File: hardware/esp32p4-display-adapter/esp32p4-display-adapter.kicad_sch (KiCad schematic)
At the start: 5 parts, among them J1 ESP32-P4_DSI_22pin, J2 Display_30pin, U1 AP2127K-2.8, U2 AP2127K-1.8, U3 TXB0102

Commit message: Fix KiCad schematic syntax (remove comments)
KiCad 8 doesn't accept ;; comments in .kicad_sch files.
Regenerated with proper S-expression format and embedded lib_symbols.
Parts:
- removed U3: TXB0102, Package_SON:Texas_DSBGA-6_0.9x1.4mm_Layout2x3_P0.5mm, symbol Logic_LevelTranslator:TXB0102DCU
- added U3: TXB0102, Package_SO:VSSOP-8_2.3x2mm_P0.5mm, symbol Logic_LevelTranslator:TXB0102
- J1: value ESP32-P4_DSI_22pin -> ESP32-P4_DSI; footprint Connector_FFC-FPC:TE_1-84953-2_1x22-1MP_P0.50mm_Horizontal -> Connector_FFC-FPC:Hirose_FH12-22S-0.5SH_1x22-1MP_P0.50mm_Horizontal
- J2: footprint Connector_FFC-FPC:TE_1-84953-0_1x30-1MP_P0.50mm_Horizontal -> Connector_FFC-FPC:Hirose_FH12-30S-0.5SH_1x30-1MP_P0.50mm_Horizontal
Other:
- note added: "ESP32-P4 DSI to Round Display Adapter MIPI DSI Connections: J1.13/14 (CLK) -> J2.16/17 (TCP/TCN) J1.16/17 (D1) -> J2.13/14 (DIP/DIN) J1.19/20 (D0) -> J2.10/11 (DOP/DON) I2C: J1.2/3 -> J2.25/26 RESET: via U3 level shifter"
- note removed: "ESP32-P4 DSI Connector (22-pin, 0.5mm pitch) J1 - Input from ESP32-P4 DevKit"
- note removed: "Level Shifter: 3.3V ↔ 1.8V for RESET signals"
- note removed: "MIPI DSI Connections: CLK: J1.13/14 → J2.16/17 D0: J1.19/20 → J2.10/11 D1: J1.16/17 → J2.13/14"
- note removed: "Power: 3.3V → LDOs → 2.8V (VCI) + 1.8V (IOVCC)"
- note removed: "Round Display Connector (30-pin, 0.5mm pitch) J2 - Output to QT021WQT Display"

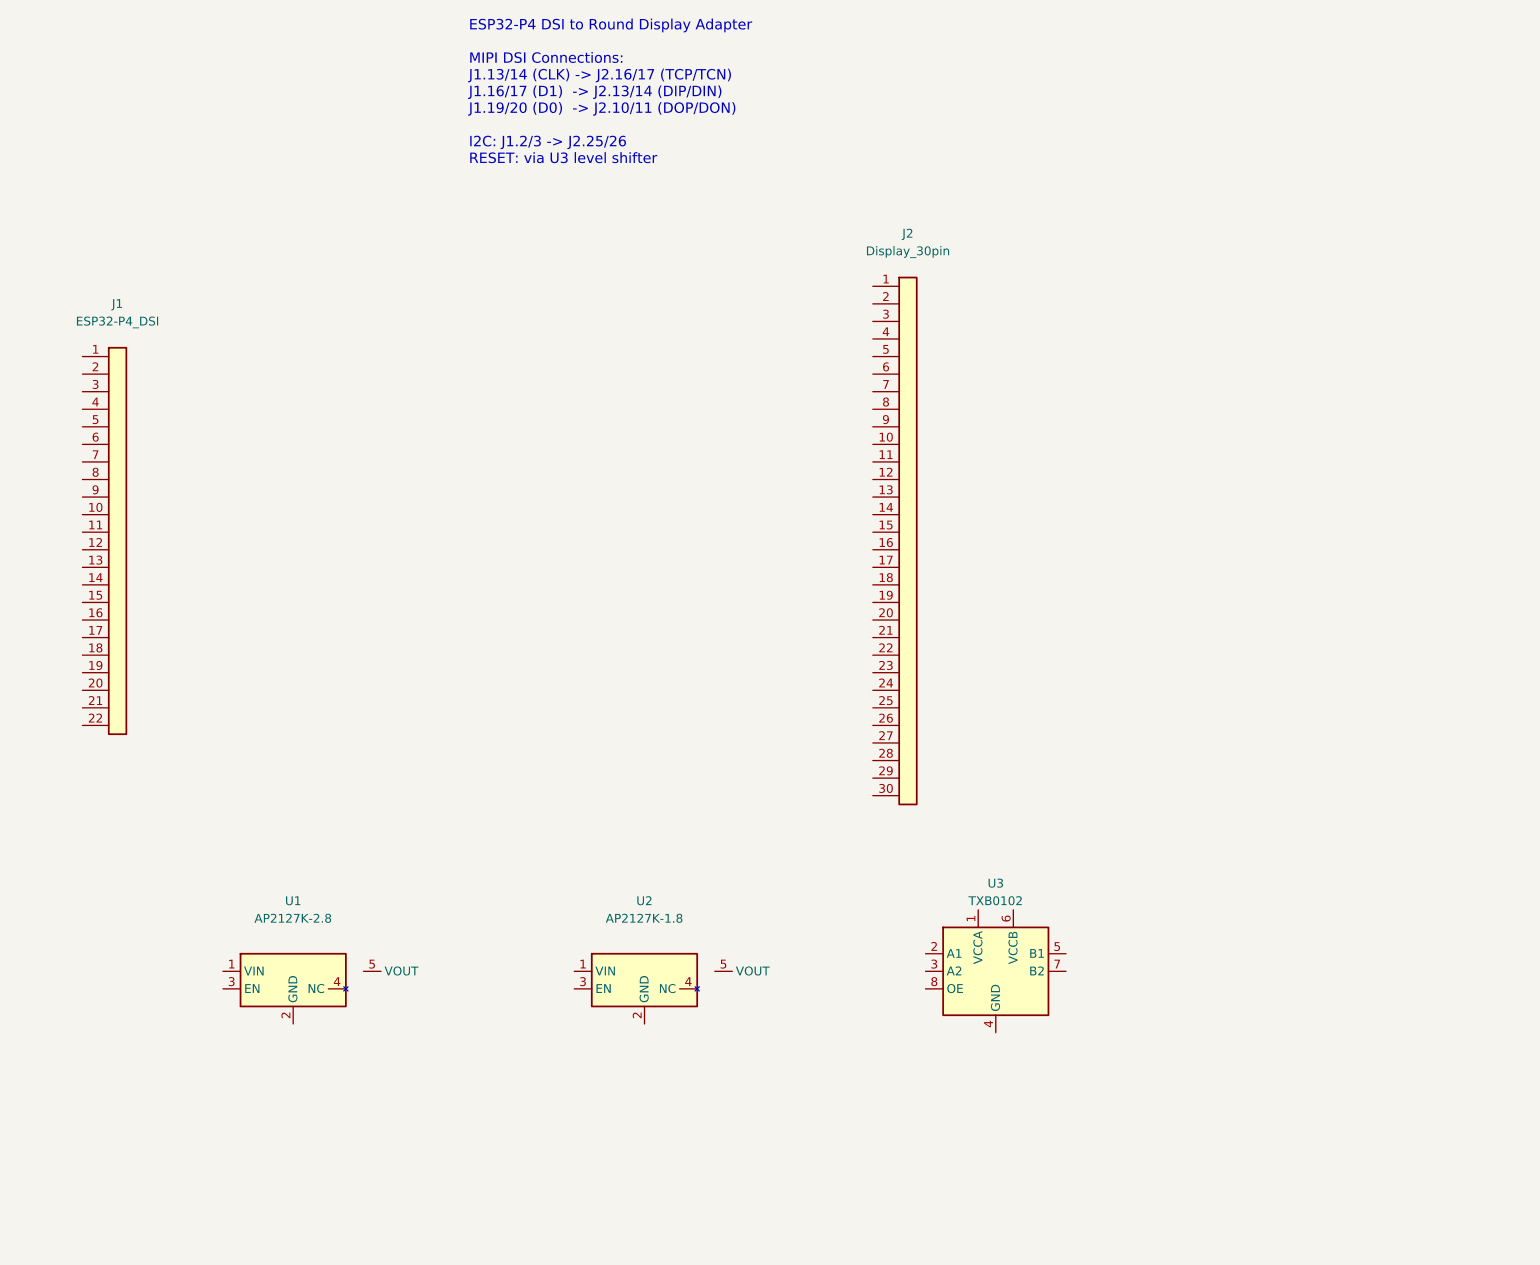
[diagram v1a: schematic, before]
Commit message: Fix ESP32-P4 DSI pinout: 15-pin 1.0mm (same as RPi)
- J1 now 15-pin 1.0mm FPC (was incorrectly 22-pin 0.5mm)
- Added J3 GPIO header for RESET/TP_RESET signals
- Updated pin mapping table to match actual pinout
- Board size 25x30mm
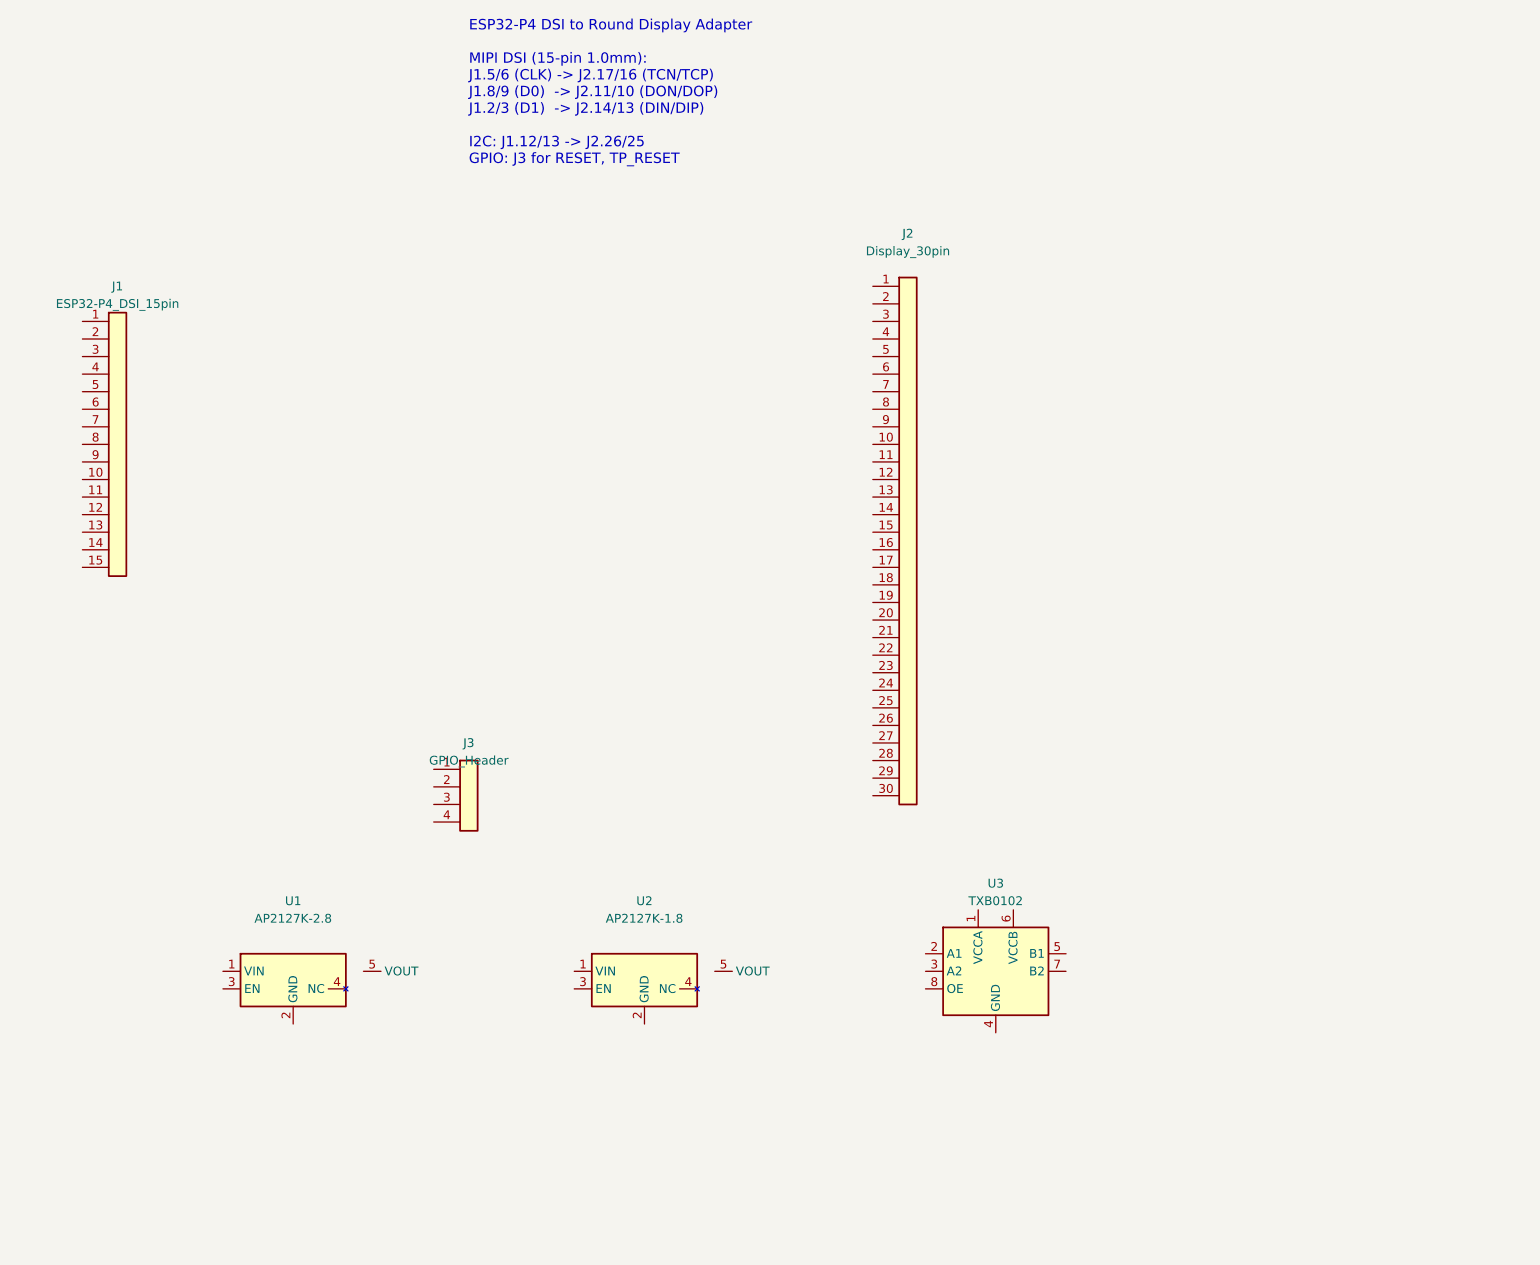
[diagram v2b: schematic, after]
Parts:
- added U3: TXB0102, Package_SO:VSSOP-8_2.3x2mm_P0.5mm, symbol Logic_LevelTranslator:TXB0102
- J1: value ESP32-P4_DSI -> ESP32-P4_DSI_15pin; footprint Connector_FFC-FPC:Hirose_FH12-22S-0.5SH_1x22-1MP_P0.50mm_Horizontal -> Connector_FFC-FPC:Hirose_FH12-15S-1.0SH_1x15-1MP_P1.00mm_Horizontal; symbol Connector_Generic:Conn_01x22 -> Connector_Generic:Conn_01x15
- J3: renamed from U1; value AP2127K-2.8 -> GPIO_Header; footprint Package_TO_SOT_SMD:SOT-23-5 -> Connector_PinHeader_2.54mm:PinHeader_1x04_P2.54mm_Vertical; symbol Regulator_Linear:AP2127K-2.8 -> Connector_Generic:Conn_01x04
- U1: renamed from U2; value AP2127K-1.8 -> AP2127K-2.8; symbol Regulator_Linear:AP2127K-1.8 -> Regulator_Linear:AP2127K-2.8
- U2: renamed from U3; value TXB0102 -> AP2127K-1.8; footprint Package_SO:VSSOP-8_2.3x2mm_P0.5mm -> Package_TO_SOT_SMD:SOT-23-5; symbol Logic_LevelTranslator:TXB0102 -> Regulator_Linear:AP2127K-1.8
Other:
- note added: "ESP32-P4 DSI to Round Display Adapter MIPI DSI (15-pin 1.0mm): J1.5/6 (CLK) -> J2.17/16 (TCN/TCP) J1.8/9 (D0) -> J2.11/10 (DON/DOP) J1.2/3 (D1) -> J2.14/13 (DIN/DIP) I2C: J1.12/13 -> J2.26/25 GPIO: J3 for RESET, TP_RESET"
- note removed: "ESP32-P4 DSI to Round Display Adapter MIPI DSI Connections: J1.13/14 (CLK) -> J2.16/17 (TCP/TCN) J1.16/17 (D1) -> J2.13/14 (DIP/DIN) J1.19/20 (D0) -> J2.10/11 (DOP/DON) I2C: J1.2/3 -> J2.25/26 RESET: via U3 level shifter"
- moved on the sheet: U1
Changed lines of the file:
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@@
     (title "ESP32-P4 DSI to Round Display Adapter")
     (date "2026-04-24")
-    (rev "1.0")
+    (rev "1.1")
     (company "bimmerz.app / OpenCluster")
   )
   (symbol
-    (lib_id "Connector_Generic:Conn_01x22")
-    (at 38.1 88.9 0)
+    (lib_id "Connector_Generic:Conn_01x15")
+    (at 38.1 76.2 0)
     (unit 1)
     (exclude_from_sim no)
@@
     (on_board yes)
     (dnp no)
-    (property "Reference" "J1" (at 38.1 55.88 0) (effects (font (size 1.27 1.27))))
-    (property "Value" "ESP32-P4_DSI" (at 38.1 58.42 0) (effects (font (size 1.27 1.27))))
-    (property "Footprint" "Connector_FFC-FPC:Hirose_FH12-22S-0.5SH_1x22-1MP_P0.50mm_Horizontal" (at 38.1 88.9 0) (effects (font (size 1.27 1.27)) hide))
+    (property "Reference" "J1" (at 38.1 53.34 0) (effects (font (size 1.27 1.27))))
+    (property "Value" "ESP32-P4_DSI_15pin" (at 38.1 55.88 0) (effects (font (size 1.27 1.27))))
+    (property "Footprint" "Connector_FFC-FPC:Hirose_FH12-15S-1.0SH_1x15-1MP_P1.00mm_Horizontal" (at 38.1 76.2 0) (effects (font (size 1.27 1.27)) hide))
     (pin "1")
     (pin "2")
@@
     (pin "14")
     (pin "15")
-    (pin "16")
-    (pin "17")
-    (pin "18")
-    (pin "19")
-    (pin "20")
-    (pin "21")
-    (pin "22")
     (instances
       (project "esp32p4-display-adapter"
@@
       (project "esp32p4-display-adapter"
         (path "/a1b2c3d4-e5f6-7890-abcd-ef1234567890" (reference "J2") (unit 1))
+      )
+    )
+  )
+  (symbol
+    (lib_id "Connector_Generic:Conn_01x04")
+    (at 88.9 127 0)
+    (unit 1)
+    (exclude_from_sim no)
+    (in_bom yes)
+    (on_board yes)
+    (dnp no)
+    (property "Reference" "J3" (at 88.9 119.38 0) (effects (font (size 1.27 1.27))))
+    (property "Value" "GPIO_Header" (at 88.9 121.92 0) (effects (font (size 1.27 1.27))))
+    (property "Footprint" "Connector_PinHeader_2.54mm:PinHeader_1x04_P2.54mm_Vertical" (at 88.9 127 0) (effects (font (size 1.27 1.27)) hide))
+    (pin "1")
+    (pin "2")
+    (pin "3")
+    (pin "4")
+    (instances
+      (project "esp32p4-display-adapter"
+        (path "/a1b2c3d4-e5f6-7890-abcd-ef1234567890" (reference "J3") (unit 1))
       )
     )
@@
     )
   )
-  (text "ESP32-P4 DSI to Round Display Adapter\n\nMIPI DSI Connections:\nJ1.13/14 (CLK) -> J2.16/17 (TCP/TCN)\nJ1.16/17 (D1)  -> J2.13/14 (DIP/DIN)\nJ1.19/20 (D0)  -> J2.10/11 (DOP/DON)\n\nI2C: J1.2/3 -> J2.25/26\nRESET: via U3 level shifter"
+  (text "ESP32-P4 DSI to Round Display Adapter\n\nMIPI DSI (15-pin 1.0mm):\nJ1.5/6 (CLK) -> J2.17/16 (TCN/TCP)\nJ1.8/9 (D0)  -> J2.11/10 (DON/DOP)\nJ1.2/3 (D1)  -> J2.14/13 (DIN/DIP)\n\nI2C: J1.12/13 -> J2.26/25\nGPIO: J3 for RESET, TP_RESET"
     (exclude_from_sim no)
     (at 88.9 25.4 0)
